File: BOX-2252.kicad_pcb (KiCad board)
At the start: 2 copper layers, 50.5 x 70 mm, 65 parts, among them P1 MYSX_1.5, P2 CONN_02X03, P3 CONN_01X03, P4 CONN_01X03, Q1 DMP3056L-7, Q2 DMP3056L-7, U1 LD1117DT33TR, U2 TPS61097A, U3 ATSHA204A, U4 RFM69HW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

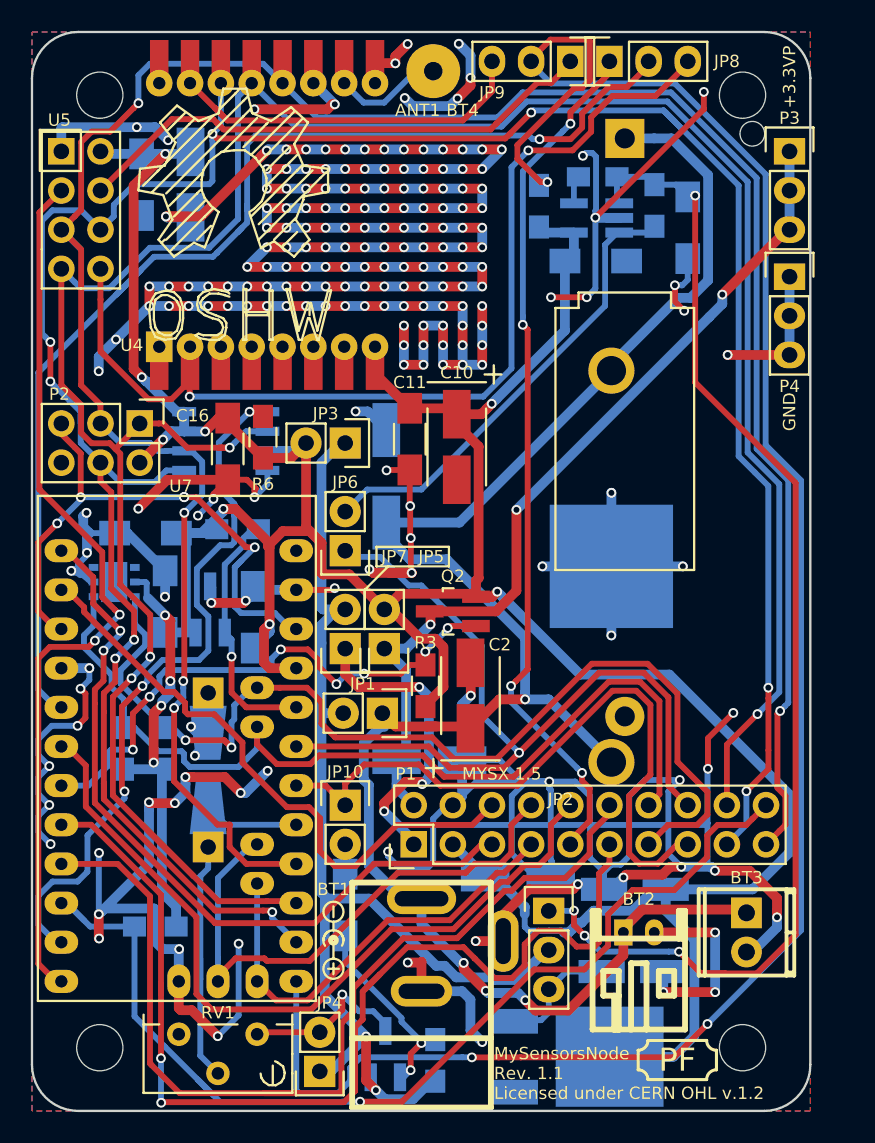
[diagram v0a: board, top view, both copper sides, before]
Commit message: Adjusted track width of some power-nets
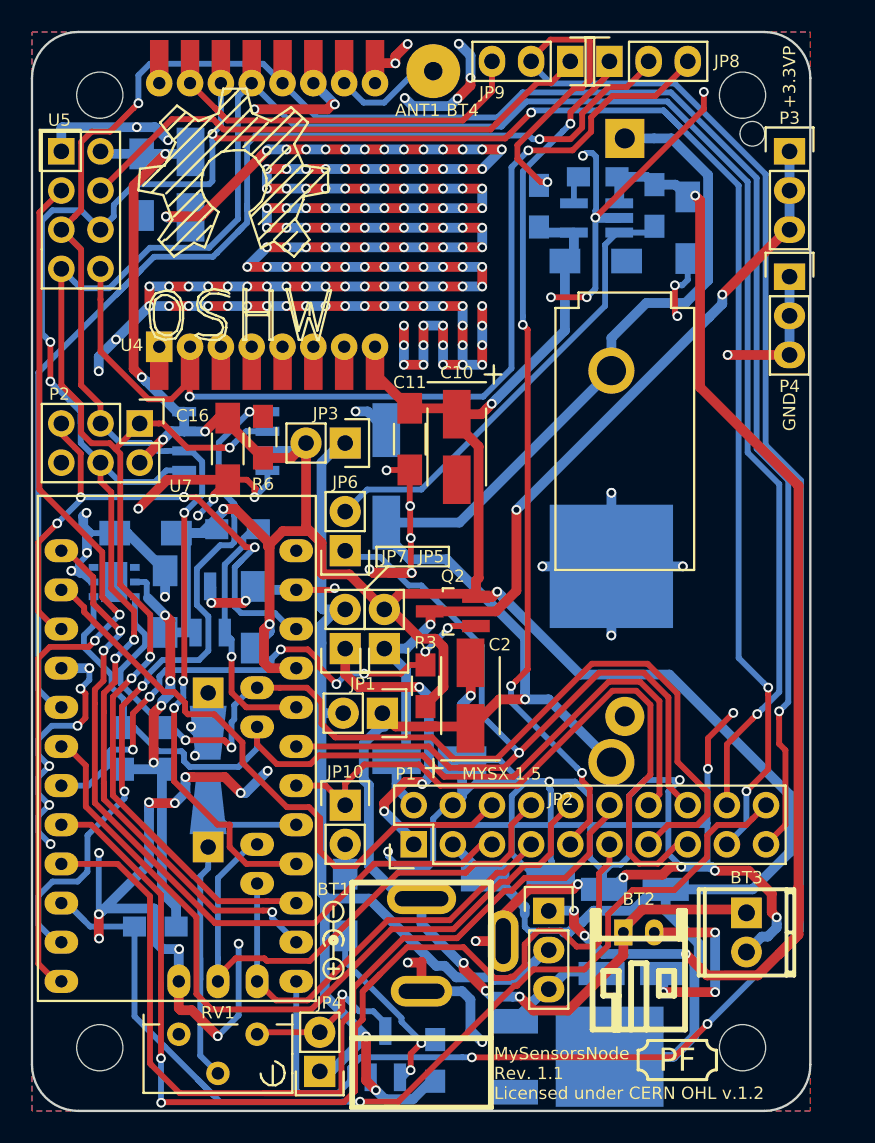
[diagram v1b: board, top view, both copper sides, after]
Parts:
- moved C4 0.13 mm to (160.3, 111.6)
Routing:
- net Net-(C5-Pad1): track 78.9 -> 88.5 mm
- net Net-(C4-Pad1): track 7.89 -> 7.06 mm

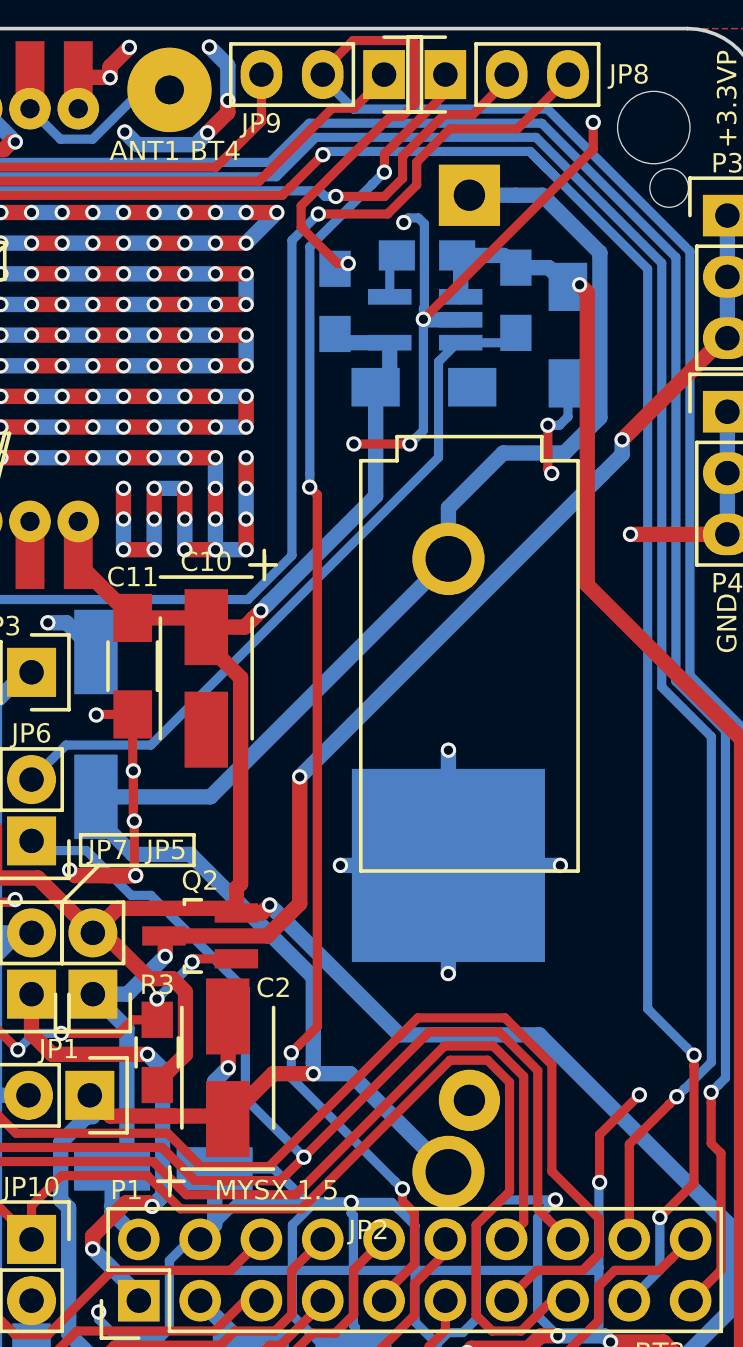
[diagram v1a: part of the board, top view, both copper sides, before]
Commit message: Added a step-up reg and some sourcing details
Added TI TPS61221 (3.3V fixed) as an alternative to TPS61097A.
Also added some more sourcing details to some components in the
schematic.
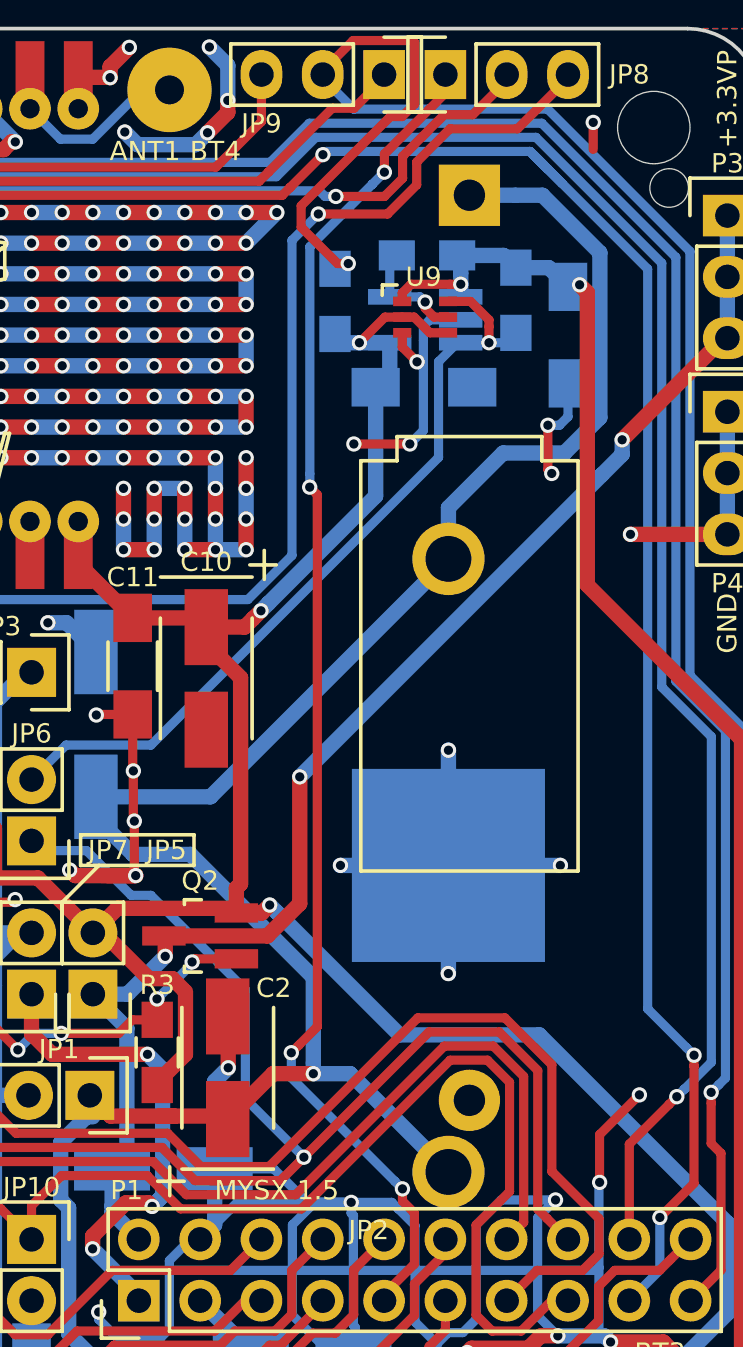
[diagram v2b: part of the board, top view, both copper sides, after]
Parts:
- added U9: TPS6122X, Housings_SOT-23_SOT-143_TSOT-6:SC-70-6, F.Cu at (157.9, 62.4)
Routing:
- net GND: track 546.4 -> 532.0 mm, vias 211 -> 209
- net +3V3: track 256.7 -> 261.1 mm, vias 12 -> 13
- net Net-(JP6-Pad2): track 30.1 -> 33.0 mm, vias 0 -> 1
- net Net-(C5-Pad1): track 88.5 -> 91.5 mm, vias 4 -> 5
- net Net-(L1-Pad1): track 1.84 -> 4.75 mm, vias 0 -> 1
- net (no net): track 8.07 -> 9.19 mm, vias 4 -> 5

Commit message: Added more sourcing details
Also minor schematic beautifications
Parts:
- U9: value TPS6122X -> TPS61221
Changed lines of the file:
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@@
       (effects (font (size 0.8 0.8) (thickness 0.16)))
     )
-    (fp_text value TPS6122X (at 0.04064 4.191 270) (layer F.Fab)
+    (fp_text value TPS61221 (at 0.04064 4.191 270) (layer F.Fab)
       (effects (font (size 1 1) (thickness 0.15)))
     )

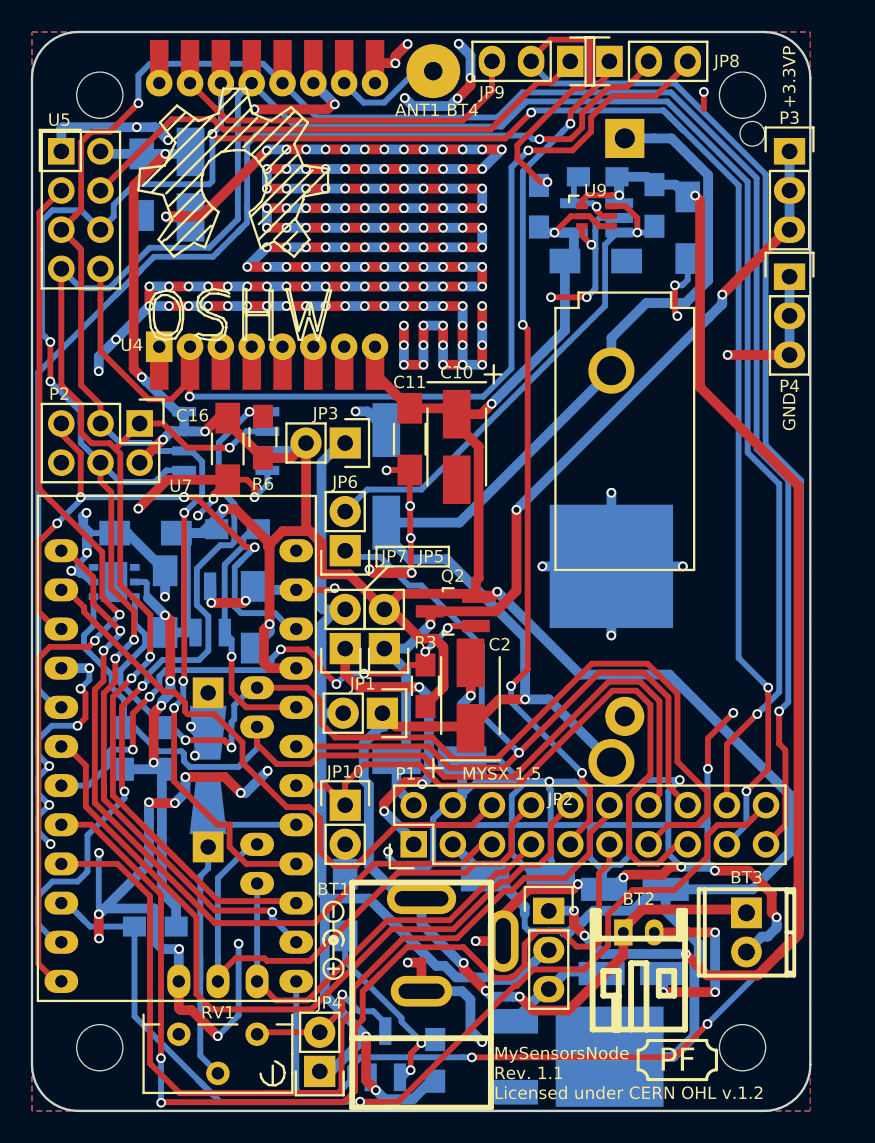
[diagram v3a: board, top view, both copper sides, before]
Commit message: Updated CR123 battery holder footprint
Fixes #11
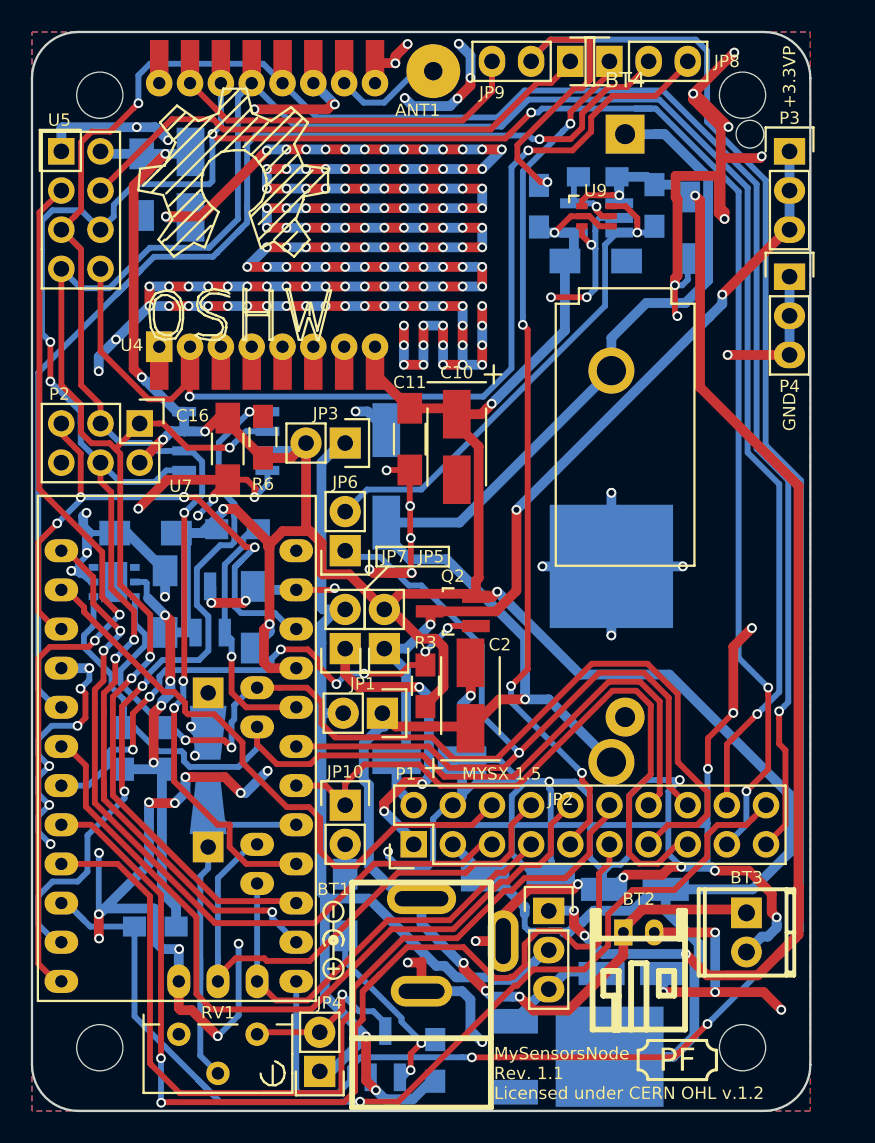
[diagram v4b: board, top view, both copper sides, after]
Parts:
- moved BT4 0.27 mm to (159.8, 57.1)
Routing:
- net GND: track 532.0 -> 574.3 mm, vias 209 -> 216
- net Net-(JP9-Pad2): track 131.2 -> 134.8 mm
- net /MOSI: track 173.0 -> 170.6 mm
- net (no net): track 9.19 -> 8.07 mm, vias 5 -> 4
- net Net-(BT1-Pad3): track 120.4 -> 121.3 mm

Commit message: Minor layout beautifications
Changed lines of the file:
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@@
     (links 186)
     (no_connects 0)
-    (area 121.235999 50.405599 171.886001 120.555601)
+    (area 114.161001 40.5024 175.904246 125.738987)
     (thickness 1.2)
     (drawings 46)
@@
     (descr "Through hole pin header")
     (tags "pin header")
-    (fp_text reference JP2 (at 0.762 -7.239) (layer F.SilkS)
+    (fp_text reference JP2 (at 0 -2.286) (layer F.SilkS)
       (effects (font (size 0.8 0.8) (thickness 0.16)))
     )
@@
     (descr "CR123 battery holder")
     (tags "Battery holder, CR123")
-    (fp_text reference BT4 (at 0 -3.5) (layer F.SilkS)
-      (effects (font (size 1 1) (thickness 0.15)))
+    (fp_text reference BT4 (at -10.414 -1.423) (layer F.SilkS)
+      (effects (font (size 0.8 0.8) (thickness 0.16)))
     )
     (fp_text value CR123 (at 0 2.54) (layer F.Fab)
